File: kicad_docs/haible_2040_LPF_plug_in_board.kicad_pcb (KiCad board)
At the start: 2 copper layers, 58.4 x 50.8 mm, 96 parts, among them J1 Conn_01x04_Male, J2 Conn_01x04_Male, J3 Conn_01x04_Male, J4 Conn_01x08_Male, Q1 BCM857DS, Q10 BCM847DS, Q11 BC847, Q12 BCM857DS, Q13 BCM847DS, Q14 BCM847DS, Q15 BC847, Q16 BCM857DS, Q17 BCM847DS, Q18 BCM847DS, Q19 BC847, Q2 BCM857DS, Q20 BC847, Q21 BC847, Q22 BC847, Q23 BC847, Q24 BC847, Q3 BCM857DS, Q4 BCM847DS, Q5 BC847, Q6 BCM847DS, Q7 BC847, Q8 BCM857DS, Q9 BCM847DS, U1 TL072, U2 TL072

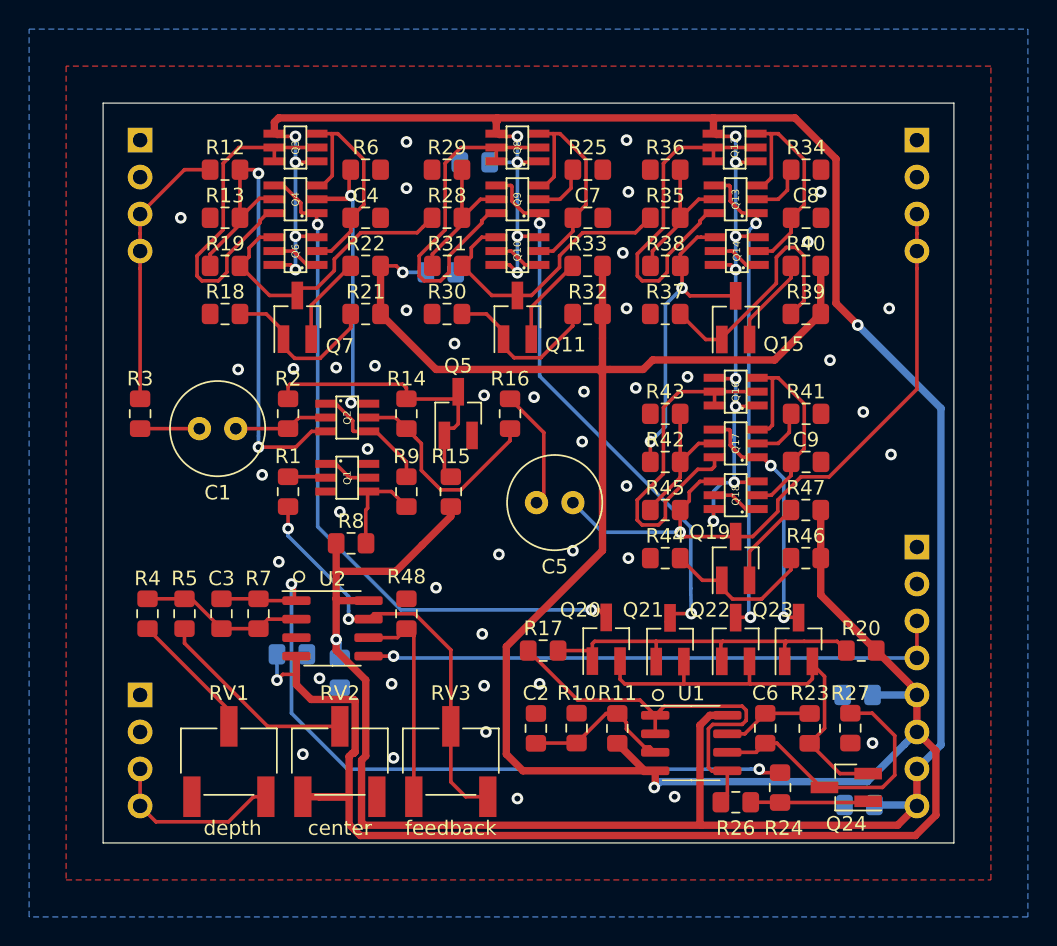
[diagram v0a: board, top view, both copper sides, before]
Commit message: split schem into pages, redo pcb
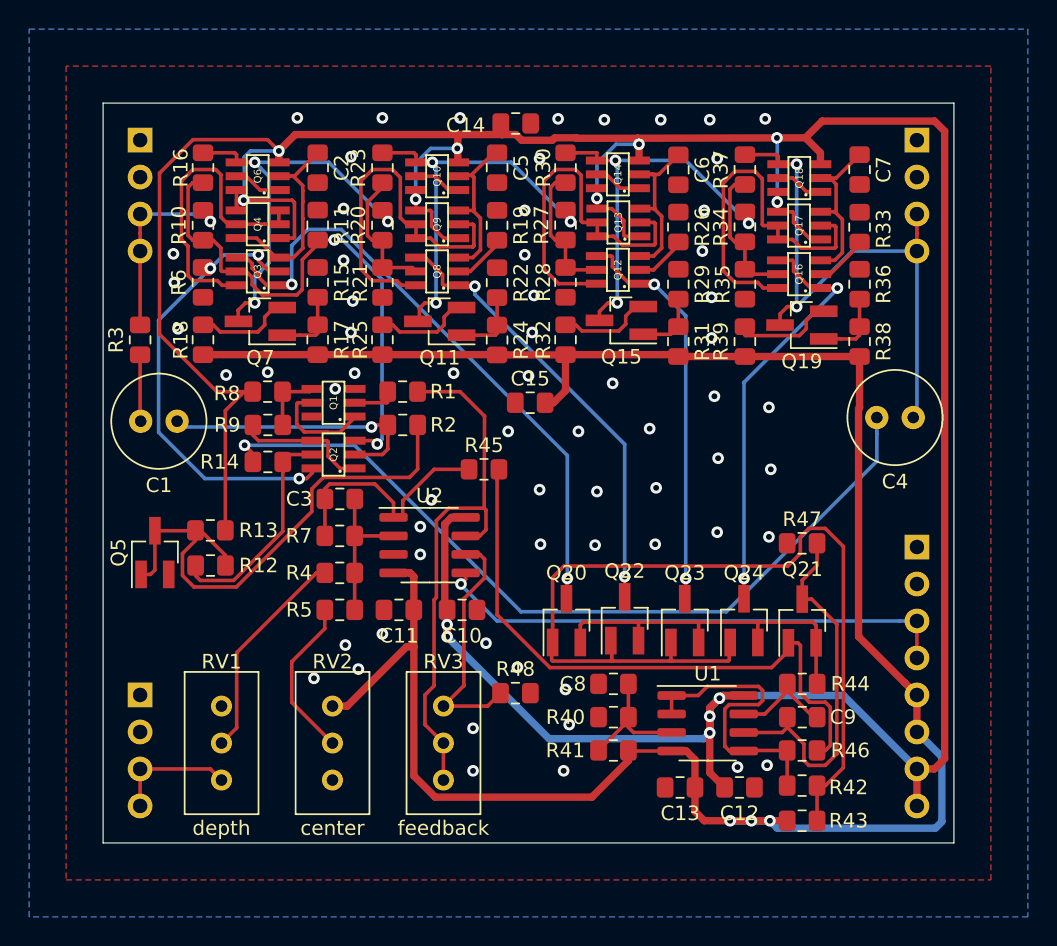
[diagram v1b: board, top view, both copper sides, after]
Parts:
- C10, C11, C12, C13, C14, C15: moved to F.Cu
- C2: value 22uF -> 1nF
- C4: value 1nF -> 10uF; footprint Capacitor_SMD:C_0805_2012Metric_Pad1.15x1.40mm_HandSolder -> Capacitor_THT:C_Radial_D6.3mm_H11.0mm_P2.50mm
- C5: value 10uF -> 1nF; footprint Capacitor_THT:C_Radial_D6.3mm_H11.0mm_P2.50mm -> Capacitor_SMD:C_0805_2012Metric_Pad1.15x1.40mm_HandSolder
- C6: value 2n2 -> 1nF
- C8: value 1nF -> 22uF
- C9: value 1nF -> 2n2
- Q12, Q16, Q3, Q8: value BCM857DS -> BCM847DS
- Q13, Q17, Q4, Q9: value BCM847DS -> BCM857DS
- R10: value 12k -> 10k
- R11: value 120k -> 220
- R12: value 10k -> 1k
- R13: value 220 -> 12k
- R14: value 1k -> 20k
- R15: value 12k -> 120k
- R16: value 20k -> 10k
- R17: value 100 -> 12k
- R18: value 120k -> 1k2
- R19, R28, R35: value 10k -> 220
- R20: value 180k -> 10k
- R21: value 12k -> 220
- R22: value 1k2 -> 120k
- R23: value 2k2 -> 10k
- R24: value 51k -> 12k
- R25: value 220 -> 1k2
- R26: value 1k -> 220
- R27: value 100k -> 10k
- R29, R36, R41: value 220 -> 120k
- R30, R37: value 120k -> 10k
- R31, R38: value 10k -> 12k
- R32, R39: value 12k -> 1k2
- R33: value 1k2 -> 220
- R34: value 220 -> 10k
- R40: value 1k2 -> 12k
- R42: value 10k -> 100
- R43: value 220 -> 180k
- R44: value 120k -> 2k2
- R45: value 10k -> 51k
- R46: value 12k -> 1k
- R47: value 1k2 -> 100k
- RV1, RV2, RV3: footprint Potentiometer_SMD:Potentiometer_Bourns_3269W_Vertical -> Potentiometer_THT:Potentiometer_Bourns_3296W_Vertical
- moved R23 48.4 mm to (120.8, 80.6)
- moved C12 46.6 mm to (145.3, 123.2), turned to 0 degrees
- moved R20 44.0 mm to (120.8, 84.6), turned to 90 degrees
- moved R10 43.0 mm to (108.5, 84.6), turned to 90 degrees
- moved C2 41.3 mm to (116.3, 80.6)
- moved R11 40.2 mm to (116.3, 84.6), turned to 90 degrees
- moved C4 40.0 mm to (157.2, 97.8), turned to 180 degrees
- moved R27 39.7 mm to (133.3, 84.6)
- moved R26 39.7 mm to (141.1, 84.7), turned to 90 degrees
- moved C14 39.6 mm to (129.9, 77.6), turned to 0 degrees
- moved C13 39.0 mm to (141.2, 123.2), turned to 0 degrees
- moved C6 38.8 mm to (141.1, 80.8), turned to 270 degrees
- moved R24 36.4 mm to (128.7, 92.5)
- moved C8 34.6 mm to (136.6, 116.1)
- moved R40 33.7 mm to (136.6, 118.4)
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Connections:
- net rez_CV renamed /FB_CV
- C2 pad 1: GND -> Net-(C2-Pad1)
- C2 pad 2: Net-(C2-Pad2) -> GND
- C3 pad 2: Net-(C3-Pad2) -> /bias_current_gen/CV_in
- C4 pad 1: Net-(C4-Pad1) -> /LP_stage_1/FB_signal_in
- C4 pad 2: GND -> Net-(C4-Pad2)
- C5 pad 2: Net-(C5-Pad2) -> GND
- C6 pad 2: Net-(C6-Pad2) -> GND
- C8 pad 1: Net-(C8-Pad1) -> GND
- C8 pad 2: GND -> Net-(C8-Pad2)
- C9 pad 2: GND -> Net-(C9-Pad2)
- J2 pad 3: Net-(J2-Pad3) -> /LP_stage_1/LP_in_1
- J2 pad 4: Net-(J2-Pad3) -> /LP_stage_1/LP_in_1
- J3 pad 3: Net-(C5-Pad1) -> /LP_stage_1/FB_signal_in
- J3 pad 4: Net-(C5-Pad1) -> /LP_stage_1/FB_signal_in
- Q10 pad 2: Net-(C7-Pad1) -> Net-(C5-Pad1)
- Q10 pad 4: Net-(Q10-Pad4) -> /LP_stage_3/LP_in_3
- Q11 pad 3: Net-(Q10-Pad4) -> /LP_stage_3/LP_in_3
- Q12 pad 1: +12V -> /LP_stage_3/bias_current_in_3
- Q12 pad 3: Net-(C8-Pad1) -> Net-(C6-Pad1)
- Q12 pad 4: +12V -> /LP_stage_3/bias_current_in_3
- Q12 pad 5: Net-(Q12-Pad2) -> Net-(Q12-Pad5)
- Q12 pad 6: Net-(Q12-Pad2) -> Net-(Q12-Pad6)
- Q13 pad 1: Net-(Q13-Pad1) -> +12V
- Q13 pad 2: Net-(Q13-Pad2) -> Net-(Q12-Pad6)
- Q13 pad 3: Net-(C8-Pad1) -> Net-(C6-Pad1)
- Q13 pad 4: Net-(Q13-Pad1) -> +12V
- Q13 pad 5: Net-(Q13-Pad5) -> Net-(Q12-Pad6)
- Q13 pad 6: Net-(Q12-Pad2) -> Net-(Q12-Pad6)
- Q14 pad 2: Net-(C8-Pad1) -> Net-(C6-Pad1)
- Q14 pad 4: Net-(Q14-Pad4) -> /LP_stage_4/LP_in_4
- Q15 pad 3: Net-(Q14-Pad4) -> /LP_stage_4/LP_in_4
- Q16 pad 1: +12V -> /LP_stage_4/bias_current_in_4
- Q16 pad 3: Net-(C9-Pad1) -> Net-(C7-Pad1)
- Q16 pad 4: +12V -> /LP_stage_4/bias_current_in_4
- Q16 pad 5: Net-(Q16-Pad2) -> Net-(Q16-Pad5)
- Q16 pad 6: Net-(Q16-Pad2) -> Net-(Q16-Pad6)
- Q17 pad 1: Net-(Q17-Pad1) -> +12V
- Q17 pad 2: Net-(Q17-Pad2) -> Net-(Q16-Pad6)
- Q17 pad 3: Net-(C9-Pad1) -> Net-(C7-Pad1)
- Q17 pad 4: Net-(Q17-Pad1) -> +12V
- Q17 pad 5: Net-(Q17-Pad5) -> Net-(Q16-Pad6)
- Q17 pad 6: Net-(Q16-Pad2) -> Net-(Q16-Pad6)
- Q18 pad 2: Net-(C9-Pad1) -> Net-(C7-Pad1)
- Q18 pad 4: Net-(C5-Pad1) -> /LP_stage_1/FB_signal_in
- Q19 pad 3: Net-(C5-Pad1) -> /LP_stage_1/FB_signal_in
- Q20 pad 3: Net-(Q20-Pad3) -> /LP_stage_1/bias_current_in_1
- Q21 pad 1: Net-(Q20-Pad1) -> Net-(Q21-Pad1)
- Q21 pad 3: Net-(Q21-Pad3) -> Net-(C9-Pad1)
- Q22 pad 3: Net-(Q13-Pad1) -> /LP_stage_2/bias_current_in_2
- Q23 pad 3: Net-(Q17-Pad1) -> /LP_stage_3/bias_current_in_3
- Q24 pad 1: Net-(Q24-Pad1) -> Net-(Q20-Pad1)
- Q24 pad 3: Net-(C6-Pad1) -> /LP_stage_4/bias_current_in_4
- Q3 pad 1: +12V -> /LP_stage_1/bias_current_in_1
- Q3 pad 2: Net-(Q3-Pad2) -> Net-(Q2-Pad6)
- Q3 pad 3: Net-(C4-Pad1) -> Net-(C2-Pad1)
- Q3 pad 4: +12V -> /LP_stage_1/bias_current_in_1
- Q3 pad 5: Net-(Q3-Pad2) -> Net-(Q2-Pad3)
- Q3 pad 6: Net-(Q3-Pad2) -> Net-(Q3-Pad6)
- Q4 pad 1: Net-(Q20-Pad3) -> +12V
- Q4 pad 2: Net-(Q2-Pad6) -> Net-(Q3-Pad6)
- Q4 pad 3: Net-(C4-Pad1) -> Net-(Q3-Pad6)
- Q4 pad 4: Net-(Q20-Pad3) -> +12V
- Q4 pad 5: Net-(Q2-Pad3) -> Net-(Q3-Pad6)
- Q4 pad 6: Net-(Q3-Pad2) -> Net-(C2-Pad1)
- Q6 pad 2: Net-(C4-Pad1) -> Net-(C2-Pad1)
- Q6 pad 4: Net-(Q6-Pad4) -> /LP_stage_2/LP_in_2
- Q7 pad 3: Net-(Q6-Pad4) -> /LP_stage_2/LP_in_2
- Q8 pad 1: +12V -> /LP_stage_2/bias_current_in_2
- Q8 pad 3: Net-(C7-Pad1) -> Net-(C5-Pad1)
- Q8 pad 4: +12V -> /LP_stage_2/bias_current_in_2
- Q8 pad 5: Net-(Q8-Pad2) -> Net-(Q8-Pad5)
- Q8 pad 6: Net-(Q8-Pad2) -> Net-(Q8-Pad6)
- Q9 pad 1: Net-(Q21-Pad3) -> +12V
- Q9 pad 2: Net-(Q9-Pad2) -> Net-(Q8-Pad6)
- Q9 pad 3: Net-(C7-Pad1) -> Net-(C5-Pad1)
- Q9 pad 4: Net-(Q21-Pad3) -> +12V
- Q9 pad 5: Net-(Q9-Pad5) -> Net-(Q8-Pad6)
- Q9 pad 6: Net-(Q8-Pad2) -> Net-(Q8-Pad6)
- R10 pad 1: GND -> Net-(Q2-Pad3)
- R10 pad 2: Net-(C2-Pad2) -> /LP_stage_1/LP_in_1
- R11 pad 1: Net-(C2-Pad2) -> Net-(Q2-Pad3)
- R11 pad 2: -12V -> GND
- R12 pad 1: Net-(Q2-Pad3) -> Net-(Q5-Pad1)
- R12 pad 2: Net-(J2-Pad3) -> Net-(Q2-Pad5)
- R13 pad 1: Net-(Q2-Pad3) -> +12V
- R13 pad 2: GND -> Net-(Q5-Pad1)
- R14 pad 1: Net-(Q5-Pad1) -> Net-(C4-Pad2)
- R15 pad 1: +12V -> GND
- R15 pad 2: Net-(Q5-Pad1) -> Net-(Q7-Pad1)
- R16 pad 1: Net-(C5-Pad2) -> /LP_stage_2/LP_in_2
- R16 pad 2: Net-(Q2-Pad5) -> Net-(Q2-Pad3)
- R17 pad 1: Net-(R17-Pad1) -> Net-(Q7-Pad1)
- R17 pad 2: Net-(Q20-Pad1) -> -12V
- R18 pad 1: GND -> Net-(Q7-Pad2)
- R18 pad 2: Net-(Q7-Pad1) -> -12V
- R19 pad 1: Net-(Q6-Pad4) -> Net-(Q8-Pad2)
- R19 pad 2: Net-(Q2-Pad3) -> GND
- R20 pad 1: -12V -> Net-(Q8-Pad5)
- R20 pad 2: Net-(Q20-Pad1) -> /LP_stage_2/LP_in_2
- R21 pad 1: Net-(Q7-Pad1) -> Net-(Q8-Pad5)
- R21 pad 2: -12V -> GND
- R22 pad 1: Net-(Q7-Pad2) -> GND
- R22 pad 2: -12V -> Net-(Q11-Pad1)
- R23 pad 1: Net-(C6-Pad2) -> /LP_stage_3/LP_in_3
- R23 pad 2: Net-(Q20-Pad2) -> Net-(Q8-Pad5)
- R24 pad 1: Net-(C3-Pad2) -> Net-(Q11-Pad1)
- R24 pad 2: Net-(Q24-Pad1) -> -12V
- R25 pad 1: Net-(Q9-Pad2) -> Net-(Q11-Pad2)
- R25 pad 2: GND -> -12V
- R26 pad 1: Net-(R17-Pad1) -> Net-(Q12-Pad2)
- R26 pad 2: Net-(Q24-Pad1) -> GND
- R27 pad 1: GND -> Net-(Q12-Pad5)
- R27 pad 2: Net-(C6-Pad1) -> /LP_stage_3/LP_in_3
- R28 pad 1: Net-(Q9-Pad5) -> Net-(Q12-Pad5)
- R28 pad 2: Net-(Q6-Pad4) -> GND
- R29 pad 1: Net-(Q9-Pad5) -> GND
- R29 pad 2: GND -> Net-(Q15-Pad1)
- R3 pad 2: Net-(J2-Pad3) -> /LP_stage_1/LP_in_1
- R30 pad 1: GND -> /LP_stage_4/LP_in_4
- R30 pad 2: Net-(Q11-Pad1) -> Net-(Q12-Pad5)
- R31 pad 1: Net-(Q10-Pad4) -> Net-(Q15-Pad1)
- R31 pad 2: Net-(Q9-Pad5) -> -12V
- R32 pad 1: Net-(Q11-Pad1) -> Net-(Q15-Pad2)
- R33 pad 1: Net-(Q11-Pad2) -> Net-(Q16-Pad2)
- R33 pad 2: -12V -> GND
- R34 pad 1: Net-(Q13-Pad2) -> Net-(Q16-Pad5)
- R34 pad 2: GND -> /LP_stage_4/LP_in_4
- R35 pad 1: Net-(Q13-Pad5) -> Net-(Q16-Pad5)
- R35 pad 2: Net-(Q10-Pad4) -> GND
- R36 pad 1: Net-(Q13-Pad5) -> GND
- R36 pad 2: GND -> Net-(Q19-Pad1)
- R37 pad 1: GND -> /LP_stage_1/FB_signal_in
- R37 pad 2: Net-(Q15-Pad1) -> Net-(Q16-Pad5)
- R38 pad 1: Net-(Q14-Pad4) -> Net-(Q19-Pad1)
- R38 pad 2: Net-(Q13-Pad5) -> -12V
- R39 pad 1: Net-(Q15-Pad1) -> Net-(Q19-Pad2)
- R40 pad 1: Net-(Q15-Pad2) -> GND
- R40 pad 2: -12V -> Net-(C8-Pad2)
- R41 pad 1: Net-(Q17-Pad2) -> Net-(C8-Pad2)
- R41 pad 2: GND -> -12V
- R42 pad 1: Net-(Q17-Pad5) -> Net-(R42-Pad1)
- R42 pad 2: Net-(Q14-Pad4) -> Net-(Q20-Pad1)
- R43 pad 1: Net-(Q17-Pad5) -> -12V
- R43 pad 2: GND -> Net-(Q20-Pad1)
- R44 pad 1: GND -> Net-(C9-Pad2)
- R44 pad 2: Net-(Q19-Pad1) -> Net-(Q20-Pad2)
- R45 pad 1: Net-(C5-Pad1) -> /bias_current_gen/CV_in
- R45 pad 2: Net-(Q17-Pad5) -> Net-(Q21-Pad1)
- R46 pad 1: Net-(Q19-Pad1) -> Net-(R42-Pad1)
- R46 pad 2: -12V -> Net-(Q21-Pad1)
- R47 pad 1: Net-(Q19-Pad2) -> GND
- R47 pad 2: -12V -> Net-(C9-Pad1)
- R7 pad 2: Net-(C3-Pad2) -> /bias_current_gen/CV_in
- U1 pad 1: Net-(R17-Pad1) -> Net-(R42-Pad1)
- U1 pad 2: Net-(R17-Pad1) -> Net-(R42-Pad1)
- U1 pad 3: Net-(C2-Pad2) -> Net-(C8-Pad2)
- U1 pad 5: Net-(R17-Pad1) -> Net-(R42-Pad1)
- U1 pad 6: Net-(C6-Pad1) -> Net-(C9-Pad1)
- U1 pad 7: Net-(C6-Pad2) -> Net-(C9-Pad2)
- U2 pad 1: Net-(C3-Pad2) -> /bias_current_gen/CV_in
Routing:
- net Net-(C4-Pad2): track 0.00 -> 56.8 mm, vias 0 -> 1
- net -12V: track 206.7 -> 153.5 mm
- net Net-(C3-Pad2): track 50.6 -> 0.00 mm, vias 2 -> 0
- net Net-(Q20-Pad3): track 48.5 -> 0.00 mm, vias 2 -> 0
- net /LP_stage_1/bias_current_in_1: track 0.00 -> 43.3 mm, vias 0 -> 2
- net Net-(Q21-Pad1): track 0.00 -> 42.8 mm
- net Net-(Q20-Pad1): track 23.7 -> 64.1 mm
- net /LP_stage_1/FB_signal_in: track 0.00 -> 39.9 mm, vias 0 -> 2
- net Net-(Q21-Pad3): track 38.4 -> 0.00 mm, vias 2 -> 0
- net Net-(C5-Pad1): track 46.3 -> 11.8 mm, vias 1 -> 0
- net Net-(Q13-Pad1): track 33.9 -> 0.00 mm, vias 2 -> 0
- net /LP_stage_2/bias_current_in_2: track 0.00 -> 30.8 mm, vias 0 -> 2
- net /LP_stage_4/bias_current_in_4: track 0.00 -> 29.3 mm, vias 0 -> 2
- net /LP_stage_2/LP_in_2: track 0.00 -> 28.5 mm, vias 0 -> 3
- net Net-(R17-Pad1): track 28.4 -> 0.00 mm
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
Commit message: tidy up pcb
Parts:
- moved Q20 11.1 mm to (132.3, 100.7)
- moved Q21 11.1 mm to (150.5, 100.7)
- moved Q24 11.1 mm to (146.1, 100.7)
- moved Q23 11.0 mm to (141.5, 100.7)
- moved Q22 11.0 mm to (136.8, 100.7)
- moved C8 8.44 mm to (134.6, 107.9)
- moved R40 8.44 mm to (134.6, 110.2)
- moved R41 8.44 mm to (134.6, 112.5)
- moved R42 8.44 mm to (147.6, 114.9)
- moved R43 8.44 mm to (147.6, 117.3)
- moved R46 8.44 mm to (147.6, 112.5)
- moved C9 8.44 mm to (147.6, 110.2)
- moved R44 8.44 mm to (147.6, 107.9)
- moved C12 8.44 mm to (143.3, 115.0)
- moved C13 8.44 mm to (139.2, 115.0)
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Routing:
- net Net-(Q20-Pad1): track 64.1 -> 49.3 mm
- net /LP_stage_1/bias_current_in_1: track 43.3 -> 31.6 mm
- net /LP_stage_4/bias_current_in_4: track 29.3 -> 17.6 mm
- net /LP_stage_3/bias_current_in_3: track 27.7 -> 16.7 mm
- net /LP_stage_2/bias_current_in_2: track 30.8 -> 20.6 mm
- net Net-(Q5-Pad1): track 37.3 -> 27.3 mm, vias 0 -> 2
- net +12V: track 248.0 -> 255.1 mm, vias 13 -> 12
- net Net-(Q20-Pad2): track 25.6 -> 30.1 mm
- net -12V: track 153.5 -> 150.2 mm, vias 3 -> 0
- net Net-(Q21-Pad1): track 42.8 -> 45.9 mm, vias 0 -> 2
- net Net-(C9-Pad1): track 25.6 -> 22.5 mm
- net Net-(C4-Pad2): track 56.8 -> 54.9 mm
- net /FB_CV: track 37.0 -> 35.4 mm
- net Net-(Q1-Pad2): track 2.99 -> 2.31 mm
- net Net-(C1-Pad1): track 18.8 -> 18.1 mm
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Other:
- board text added: "github.com/JordanAceto/haible_2040_LPF_plug_in_board rev 1 2020/02/02"
